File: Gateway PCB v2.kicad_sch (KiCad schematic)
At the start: 107 parts, among them J1 Conn_Coaxial, J2 Conn_01x04_Pin, J3 Conn_02x03_Odd_Even, U6 TPS7A91, U7 TLV62568ADRL, X1 TG2016SMN 32.0000M-TCGNNMB

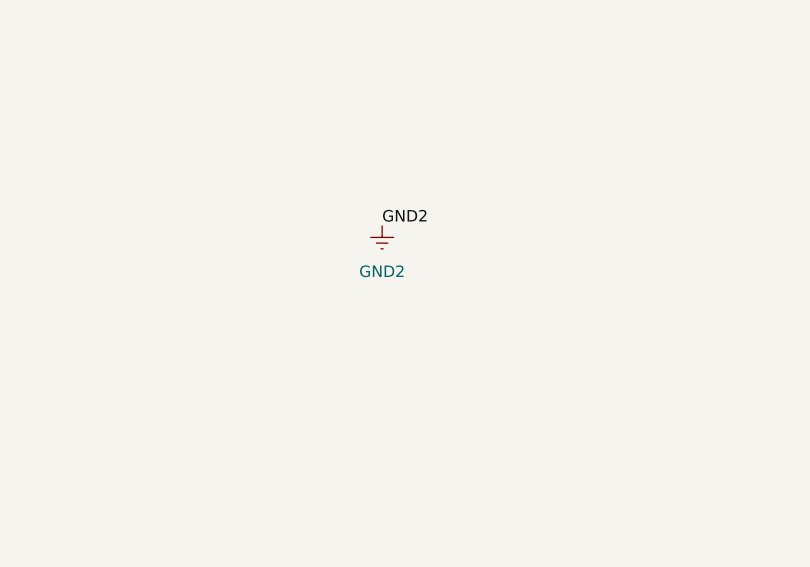
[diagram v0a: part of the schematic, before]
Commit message: re route sky
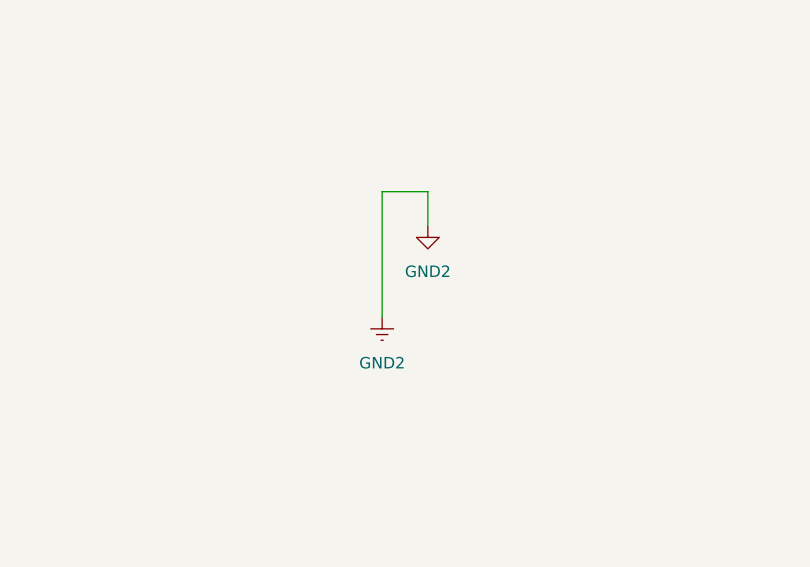
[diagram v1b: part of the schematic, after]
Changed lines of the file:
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@@
 	(wire
 		(pts
+			(xy 394.97 217.17) (xy 394.97 220.98)
+		)
+		(stroke
+			(width 0)
+			(type default)
+		)
+	)
+	(wire
+		(pts
 			(xy 290.83 279.4) (xy 290.83 284.48)
 		)
@@
 	(wire
 		(pts
+			(xy 389.89 217.17) (xy 389.89 231.14)
+		)
+		(stroke
+			(width 0)
+			(type default)
+		)
+	)
+	(wire
+		(pts
 			(xy 417.83 92.71) (xy 417.83 91.44)
 		)
@@
 	(wire
 		(pts
+			(xy 394.97 217.17) (xy 389.89 217.17)
+		)
+		(stroke
+			(width 0)
+			(type default)
+		)
+	)
+	(wire
+		(pts
 			(xy 85.09 309.88) (xy 88.9 309.88)
 		)
@@
 		)
 	)
-	(label "GND2"
-		(at 389.89 220.98 0)
-		(effects
-			(font
-				(size 1.27 1.27)
-			)
-			(justify left bottom)
-		)
-	)
 	(global_label "PA_ON"
 		(shape input)
@@
 			)
 		)
-		(property "Description" "Inductor"
+		(property "Description" "LQW15AN4N7C00D"
 			(at 353.06 83.82 0)
 			(effects
@@
 	)
 	(symbol
+		(lib_id "power:GND2")
+		(at 394.97 220.98 0)
+		(unit 1)
+		(exclude_from_sim no)
+		(in_bom yes)
+		(on_board yes)
+		(dnp no)
+		(fields_autoplaced yes)
+		(property "Reference" "#PWR028"
+			(at 394.97 227.33 0)
+			(effects
+				(font
+					(size 1.27 1.27)
+				)
+				(hide yes)
+			)
+		)
+		(property "Value" "GND2"
+			(at 394.97 226.06 0)
+			(effects
+				(font
+					(size 1.27 1.27)
+				)
+			)
+		)
+		(property "Footprint" ""
+			(at 394.97 220.98 0)
+			(effects
+				(font
+					(size 1.27 1.27)
+				)
+				(hide yes)
+			)
+		)
+		(property "Datasheet" ""
+			(at 394.97 220.98 0)
+			(effects
+				(font
+					(size 1.27 1.27)
+				)
+				(hide yes)
+			)
+		)
+		(property "Description" "Power symbol creates a global label with name \"GND2\" , ground"
+			(at 394.97 220.98 0)
+			(effects
+				(font
+					(size 1.27 1.27)
+				)
+				(hide yes)
+			)
+		)
+		(pin "1"
+		)
+		(instances
+			(project ""
+				(path "/3d6c7bcf-e42c-4747-acbc-b9f809b2c591"
+					(reference "#PWR028")
+					(unit 1)
+				)
+			)
+		)
+	)
+	(symbol
 		(lib_id "power:Earth")
 		(at 256.54 293.37 0)
@@
 	(symbol
 		(lib_id "power:Earth")
-		(at 389.89 220.98 0)
+		(at 389.89 231.14 0)
 		(unit 1)
 		(exclude_from_sim no)
@@
 		(fields_autoplaced yes)
 		(property "Reference" "#PWR021"
-			(at 389.89 227.33 0)
+			(at 389.89 237.49 0)
 			(effects
 				(font
@@
 		)
 		(property "Value" "GND2"
-			(at 389.89 226.06 0)
+			(at 389.89 236.22 0)
 			(effects
 				(font
@@
 		)
 		(property "Footprint" ""
-			(at 389.89 220.98 0)
+			(at 389.89 231.14 0)
 			(effects
 				(font
@@
 		)
 		(property "Datasheet" "~"
-			(at 389.89 220.98 0)
+			(at 389.89 231.14 0)
 			(effects
 				(font
@@
 		)
 		(property "Description" "Power symbol creates a global label with name \"Earth\""
-			(at 389.89 220.98 0)
+			(at 389.89 231.14 0)
 			(effects
 				(font

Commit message: UpDate
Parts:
- added NT1, NT2, NT3, NT4, NT5: NetTie_2, NetTie:NetTie-2_SMD_Pad0.5mm, symbol Device:NetTie_2
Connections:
- net GND2: now also NT1.1, NT1.2, NT2.1, NT2.2, NT3.1, NT3.2, NT4.1, NT4.2, NT5.1, NT5.2

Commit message: Fail Save 3
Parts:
- added NT6, NT7: NetTie_2, NetTie:NetTie-2_SMD_Pad0.5mm, symbol Device:NetTie_2
- J3: footprint Connector_PinHeader_2.54mm:PinHeader_2x03_P2.54mm_Vertical -> Connector_PinHeader_2.54mm:PinHeader_1x06_P2.54mm_Vertical
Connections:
- net EX_HOST_MISO: now also J3.3 (Pin_3); no longer J3.1 (Pin_1)
- net EX_HOST_RESET: now also J3.4 (Pin_4); no longer J3.3 (Pin_3)
- net EX_HOST_SCK: now also J3.1 (Pin_1); no longer J3.4 (Pin_4)
- net GND: now also J3.6 (Pin_6)
- new net GND3: NT6.1, NT6.2, NT7.1, NT7.2
- no-connect marks 25 -> 24
